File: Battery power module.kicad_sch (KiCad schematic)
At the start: 14 parts, among them J1 USB_C_Receptacle_PowerOnly_6P, J2 Conn_01x02, U1 BQ24090DGQ

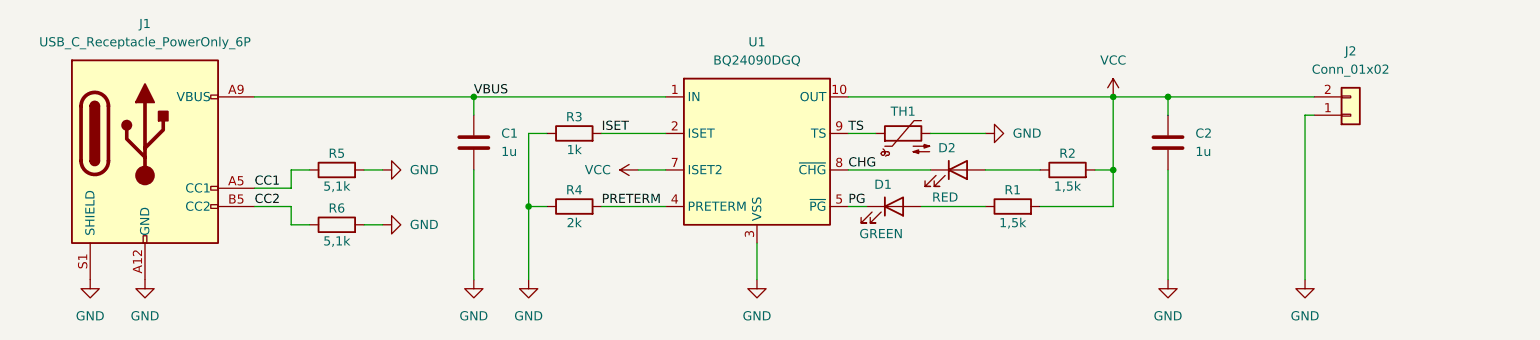
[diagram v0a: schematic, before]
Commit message: Add TVS & finish ver. 1.0
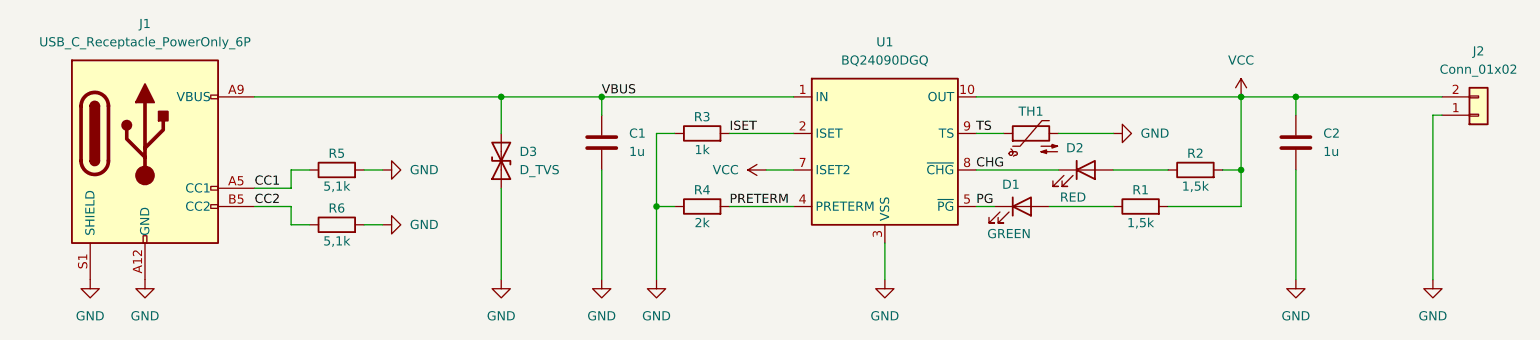
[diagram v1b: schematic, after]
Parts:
- added D3: D_TVS, Diode_SMD:D_SMB, symbol Device:D_TVS
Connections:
- net GND: now also D3.1 (A1)
- net VBUS: now also D3.2 (A2)
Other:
- moved on the sheet: C1, C2, D1, D2, J2, R1, R2, R3, R4, TH1, U1
